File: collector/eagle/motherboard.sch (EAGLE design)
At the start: 9 parts

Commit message: Updated scheme of collector motherboard
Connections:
- net GND: now also U$3.LED_GREEN_-, U$3.LED_YELLOW_-
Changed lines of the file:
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@@
 <part name="U$1" library="ut-boards" deviceset="HANRUN_HR911105A_15/10" device=""/>
 <part name="U$2" library="ut-boards" deviceset="STM32F103C8T6_BOARD_BLACK" device=""/>
-<part name="U$3" library="ut-connectors" deviceset="RJHSE-5481_(RJ45)" device=""/>
 <part name="R1" library="resistor" deviceset="R-EU_" device="R1206"/>
 <part name="R2" library="resistor" deviceset="R-EU_" device="R1206"/>
@@
 <part name="R4" library="resistor" deviceset="R-EU_" device="R1206"/>
 <part name="R5" library="resistor" deviceset="R-EU_" device="R1206"/>
+<part name="U$3" library="ut-connectors" deviceset="RJHSE-5481_(RJ45)" device=""/>
 </parts>
 <sheets>
@@
 <instance part="U$1" gate="G$1" x="40.64" y="60.96" rot="R270"/>
 <instance part="U$2" gate="G$1" x="104.14" y="43.18"/>
-<instance part="U$3" gate="G$1" x="101.6" y="-35.56"/>
 <instance part="R1" gate="G$1" x="121.92" y="-12.7"/>
 <instance part="R2" gate="G$1" x="121.92" y="-10.16"/>
@@
 <instance part="R4" gate="G$1" x="76.2" y="33.02"/>
 <instance part="R5" gate="G$1" x="76.2" y="38.1"/>
+<instance part="U$3" gate="G$1" x="101.6" y="-35.56"/>
 </instances>
 <busses>
@@
 <wire x1="119.38" y1="-20.32" x2="93.98" y2="-20.32" width="0.1524" layer="91"/>
 <wire x1="93.98" y1="-20.32" x2="88.9" y2="-20.32" width="0.1524" layer="91"/>
-<wire x1="88.9" y1="-20.32" x2="88.9" y2="-22.86" width="0.1524" layer="91"/>
-<wire x1="119.38" y1="-20.32" x2="119.38" y2="-22.86" width="0.1524" layer="91"/>
 <junction x="88.9" y="-20.32"/>
 <wire x1="129.54" y1="-20.32" x2="119.38" y2="-20.32" width="0.1524" layer="91"/>
@@
 <wire x1="93.98" y1="-33.02" x2="93.98" y2="-20.32" width="0.1524" layer="91"/>
 <junction x="93.98" y="-20.32"/>
-<pinref part="U$3" gate="G$1" pin="P8"/>
 <wire x1="88.9" y1="-20.32" x2="35.56" y2="-20.32" width="0.1524" layer="91"/>
 <wire x1="35.56" y1="-20.32" x2="35.56" y2="45.72" width="0.1524" layer="91"/>
@@
 <label x="124.46" y="-22.86" size="1.778" layer="95"/>
 <label x="101.6" y="-20.32" size="1.778" layer="95"/>
+<pinref part="U$3" gate="G$1" pin="P8"/>
+<pinref part="U$3" gate="G$1" pin="LED_YELLOW_-"/>
+<wire x1="88.9" y1="-20.32" x2="88.9" y2="-27.94" width="0.1524" layer="91"/>
+<pinref part="U$3" gate="G$1" pin="LED_GREEN_-"/>
+<wire x1="119.38" y1="-20.32" x2="119.38" y2="-27.94" width="0.1524" layer="91"/>
 </segment>
 </net>
@@
 <wire x1="116.84" y1="27.94" x2="96.52" y2="27.94" width="0.1524" layer="91"/>
 <wire x1="96.52" y1="27.94" x2="96.52" y2="-2.54" width="0.1524" layer="91"/>
-<pinref part="U$3" gate="G$1" pin="P7"/>
 <wire x1="96.52" y1="-2.54" x2="96.52" y2="-35.56" width="0.1524" layer="91"/>
 <wire x1="96.52" y1="-2.54" x2="38.1" y2="-2.54" width="0.1524" layer="91"/>
@@
 <label x="76.2" y="-5.08" size="1.778" layer="95"/>
 <label x="96.52" y="-15.24" size="1.778" layer="95"/>
+<pinref part="U$3" gate="G$1" pin="P7"/>
 </segment>
 </net>
@@
 <net name="N$9" class="0">
 <segment>
-<wire x1="116.84" y1="-12.7" x2="116.84" y2="-22.86" width="0.1524" layer="91"/>
+<wire x1="116.84" y1="-12.7" x2="116.84" y2="-27.94" width="0.1524" layer="91"/>
+<pinref part="R1" gate="G$1" pin="1"/>
 <pinref part="U$3" gate="G$1" pin="LED_GREEN_+"/>
-<pinref part="R1" gate="G$1" pin="1"/>
-<wire x1="116.84" y1="-27.94" x2="116.84" y2="-22.86" width="0.1524" layer="91"/>
 </segment>
 </net>
@@
 <segment>
 <wire x1="86.36" y1="-10.16" x2="86.36" y2="-27.94" width="0.1524" layer="91"/>
-<pinref part="U$3" gate="G$1" pin="LED_YELLOW_+"/>
 <pinref part="R2" gate="G$1" pin="1"/>
 <wire x1="116.84" y1="-10.16" x2="86.36" y2="-10.16" width="0.1524" layer="91"/>
 <label x="101.6" y="-10.16" size="1.778" layer="95"/>
+<pinref part="U$3" gate="G$1" pin="LED_YELLOW_+"/>
 </segment>
 </net>
@@
 <junction x="91.44" y="58.42"/>
 <wire x1="111.76" y1="58.42" x2="111.76" y2="-35.56" width="0.1524" layer="91"/>
+<label x="111.76" y="-2.54" size="1.778" layer="95"/>
 <pinref part="U$3" gate="G$1" pin="P1"/>
-<label x="111.76" y="-2.54" size="1.778" layer="95"/>
 </segment>
 </net>
@@
 <junction x="91.44" y="55.88"/>
 <wire x1="109.22" y1="55.88" x2="109.22" y2="-33.02" width="0.1524" layer="91"/>
+<label x="104.14" y="-2.54" size="1.778" layer="95"/>
 <pinref part="U$3" gate="G$1" pin="P2"/>
-<label x="104.14" y="-2.54" size="1.778" layer="95"/>
 </segment>
 </net>

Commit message: Tiny fixes on colletor's motherboard
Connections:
- net 3V3: now also RGB_LED.4
- net GND: no longer RGB_LED.4
- net PC13: now also RGB_LED.3; no longer RGB_LED.1
- net PC15: now also RGB_LED.1; no longer RGB_LED.3
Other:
- note added: "+"
- note removed: "GND"
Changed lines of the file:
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@@
 <text x="66.04" y="17.78" size="1.778" layer="97">G</text>
 <text x="60.96" y="15.24" size="1.778" layer="97">B</text>
-<text x="66.04" y="15.24" size="1.778" layer="97">GND</text>
+<text x="65.532" y="13.716" size="1.778" layer="97">+</text>
 </plain>
 <instances>
@@
 <wire x1="129.54" y1="-20.32" x2="119.38" y2="-20.32" width="0.1524" layer="91"/>
 <junction x="119.38" y="-20.32"/>
-<pinref part="RGB_LED" gate="A" pin="4"/>
-<wire x1="66.04" y1="15.24" x2="116.84" y2="15.24" width="0.1524" layer="91"/>
-<junction x="116.84" y="15.24"/>
 <wire x1="93.98" y1="-33.02" x2="93.98" y2="-20.32" width="0.1524" layer="91"/>
 <junction x="93.98" y="-20.32"/>
@@
 <junction x="116.84" y="27.94"/>
 <wire x1="116.84" y1="27.94" x2="96.52" y2="27.94" width="0.1524" layer="91"/>
-<wire x1="96.52" y1="27.94" x2="96.52" y2="-2.54" width="0.1524" layer="91"/>
+<wire x1="96.52" y1="27.94" x2="96.52" y2="15.24" width="0.1524" layer="91"/>
+<wire x1="96.52" y1="15.24" x2="96.52" y2="-2.54" width="0.1524" layer="91"/>
 <wire x1="96.52" y1="-2.54" x2="96.52" y2="-35.56" width="0.1524" layer="91"/>
 <wire x1="96.52" y1="-2.54" x2="38.1" y2="-2.54" width="0.1524" layer="91"/>
@@
 <label x="96.52" y="-15.24" size="1.778" layer="95"/>
 <pinref part="U$3" gate="G$1" pin="P7"/>
+<pinref part="RGB_LED" gate="A" pin="4"/>
+<wire x1="96.52" y1="15.24" x2="66.04" y2="15.24" width="0.1524" layer="91"/>
+<junction x="96.52" y="15.24"/>
 </segment>
 </net>
@@
 <net name="PC13" class="0">
 <segment>
-<pinref part="RGB_LED" gate="A" pin="1"/>
-<wire x1="55.88" y1="38.1" x2="55.88" y2="17.78" width="0.1524" layer="91"/>
-<wire x1="55.88" y1="17.78" x2="58.42" y2="17.78" width="0.1524" layer="91"/>
 <pinref part="R5" gate="G$1" pin="1"/>
-<wire x1="71.12" y1="38.1" x2="55.88" y2="38.1" width="0.1524" layer="91"/>
-<label x="55.88" y="25.4" size="1.778" layer="95"/>
+<wire x1="71.12" y1="38.1" x2="53.34" y2="38.1" width="0.1524" layer="91"/>
+<wire x1="53.34" y1="38.1" x2="53.34" y2="15.24" width="0.1524" layer="91"/>
+<pinref part="RGB_LED" gate="A" pin="3"/>
+<wire x1="53.34" y1="15.24" x2="58.42" y2="15.24" width="0.1524" layer="91"/>
+<label x="55.88" y="35.56" size="1.778" layer="95"/>
 </segment>
 </net>
@@
 </segment>
 </net>
-<net name="PC15" class="0">
-<segment>
-<pinref part="RGB_LED" gate="A" pin="3"/>
-<wire x1="50.8" y1="33.02" x2="50.8" y2="15.24" width="0.1524" layer="91"/>
-<wire x1="50.8" y1="15.24" x2="58.42" y2="15.24" width="0.1524" layer="91"/>
-<pinref part="R4" gate="G$1" pin="1"/>
-<wire x1="71.12" y1="33.02" x2="50.8" y2="33.02" width="0.1524" layer="91"/>
-<label x="43.18" y="17.78" size="1.778" layer="95"/>
-</segment>
-</net>
 <net name="N$16" class="0">
 <segment>
@@
 </segment>
 </net>
+<net name="PC15" class="0">
+<segment>
+<pinref part="R4" gate="G$1" pin="1"/>
+<wire x1="71.12" y1="33.02" x2="55.88" y2="33.02" width="0.1524" layer="91"/>
+<wire x1="55.88" y1="33.02" x2="55.88" y2="17.78" width="0.1524" layer="91"/>
+<pinref part="RGB_LED" gate="A" pin="1"/>
+<wire x1="55.88" y1="17.78" x2="58.42" y2="17.78" width="0.1524" layer="91"/>
+<label x="58.42" y="30.48" size="1.778" layer="95"/>
+</segment>
+</net>

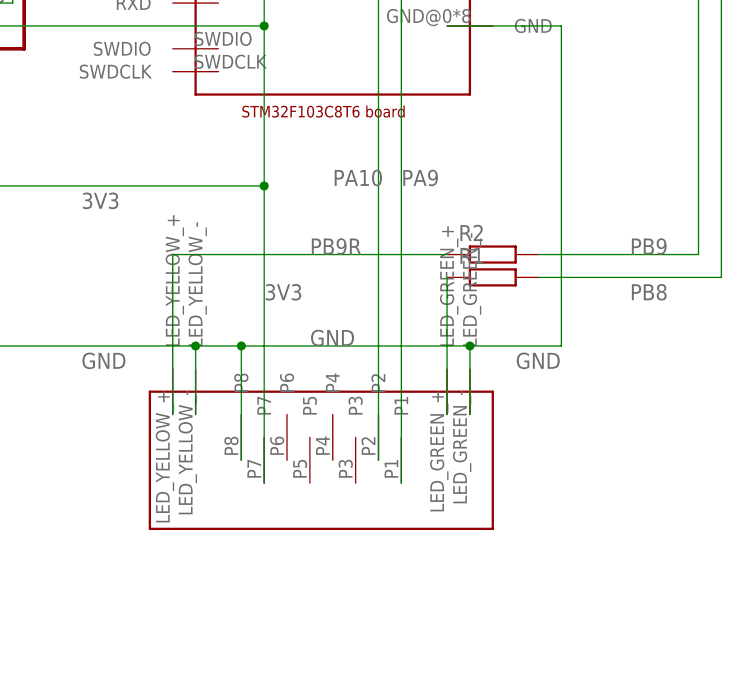
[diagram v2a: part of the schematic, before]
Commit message: Updated sensor's scheme, colletor's photo and README.md
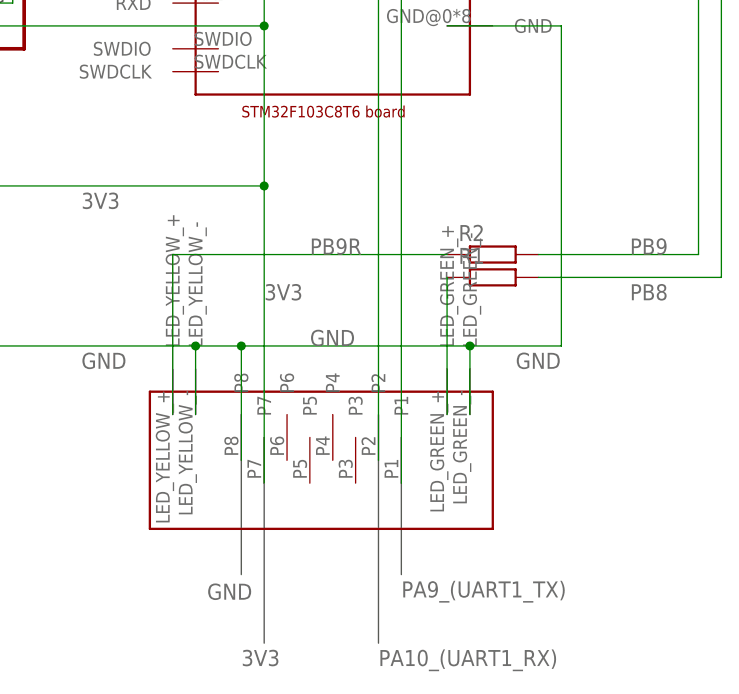
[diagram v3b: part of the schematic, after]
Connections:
- net PA10 renamed PA10_(UART1_RX)
- net PA9 renamed PA9_(UART1_TX)
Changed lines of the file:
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@@
 <text x="60.96" y="15.24" size="1.778" layer="97">B</text>
 <text x="65.532" y="13.716" size="1.778" layer="97">+</text>
+<wire x1="93.98" y1="-33.02" x2="93.98" y2="-45.72" width="0.1524" layer="97"/>
+<wire x1="96.52" y1="-53.34" x2="96.52" y2="-35.56" width="0.1524" layer="97"/>
+<wire x1="109.22" y1="-33.02" x2="109.22" y2="-53.34" width="0.1524" layer="97"/>
+<wire x1="111.76" y1="-35.56" x2="111.76" y2="-45.72" width="0.1524" layer="97"/>
 </plain>
 <instances>
@@
 <pinref part="U$3" gate="G$1" pin="LED_GREEN_-"/>
 <wire x1="119.38" y1="-20.32" x2="119.38" y2="-27.94" width="0.1524" layer="91"/>
+<label x="90.17" y="-48.514" size="1.778" layer="95"/>
 </segment>
 </net>
@@
 <wire x1="96.52" y1="15.24" x2="66.04" y2="15.24" width="0.1524" layer="91"/>
 <junction x="96.52" y="15.24"/>
+<label x="93.98" y="-55.88" size="1.778" layer="95"/>
 </segment>
 </net>
@@
 </segment>
 </net>
-<net name="PA9" class="0">
+<net name="PA9_(UART1_TX)" class="0">
 <segment>
 <pinref part="U$2" gate="G$1" pin="PA9"/>
@@
 <junction x="91.44" y="58.42"/>
 <wire x1="111.76" y1="58.42" x2="111.76" y2="-35.56" width="0.1524" layer="91"/>
-<label x="111.76" y="-2.54" size="1.778" layer="95"/>
 <pinref part="U$3" gate="G$1" pin="P1"/>
+<label x="111.76" y="-48.26" size="1.778" layer="95"/>
 </segment>
 </net>
-<net name="PA10" class="0">
+<net name="PA10_(UART1_RX)" class="0">
 <segment>
 <pinref part="U$2" gate="G$1" pin="PA10"/>
@@
 <junction x="91.44" y="55.88"/>
 <wire x1="109.22" y1="55.88" x2="109.22" y2="-33.02" width="0.1524" layer="91"/>
-<label x="104.14" y="-2.54" size="1.778" layer="95"/>
 <pinref part="U$3" gate="G$1" pin="P2"/>
+<label x="109.22" y="-55.88" size="1.778" layer="95"/>
 </segment>
 </net>

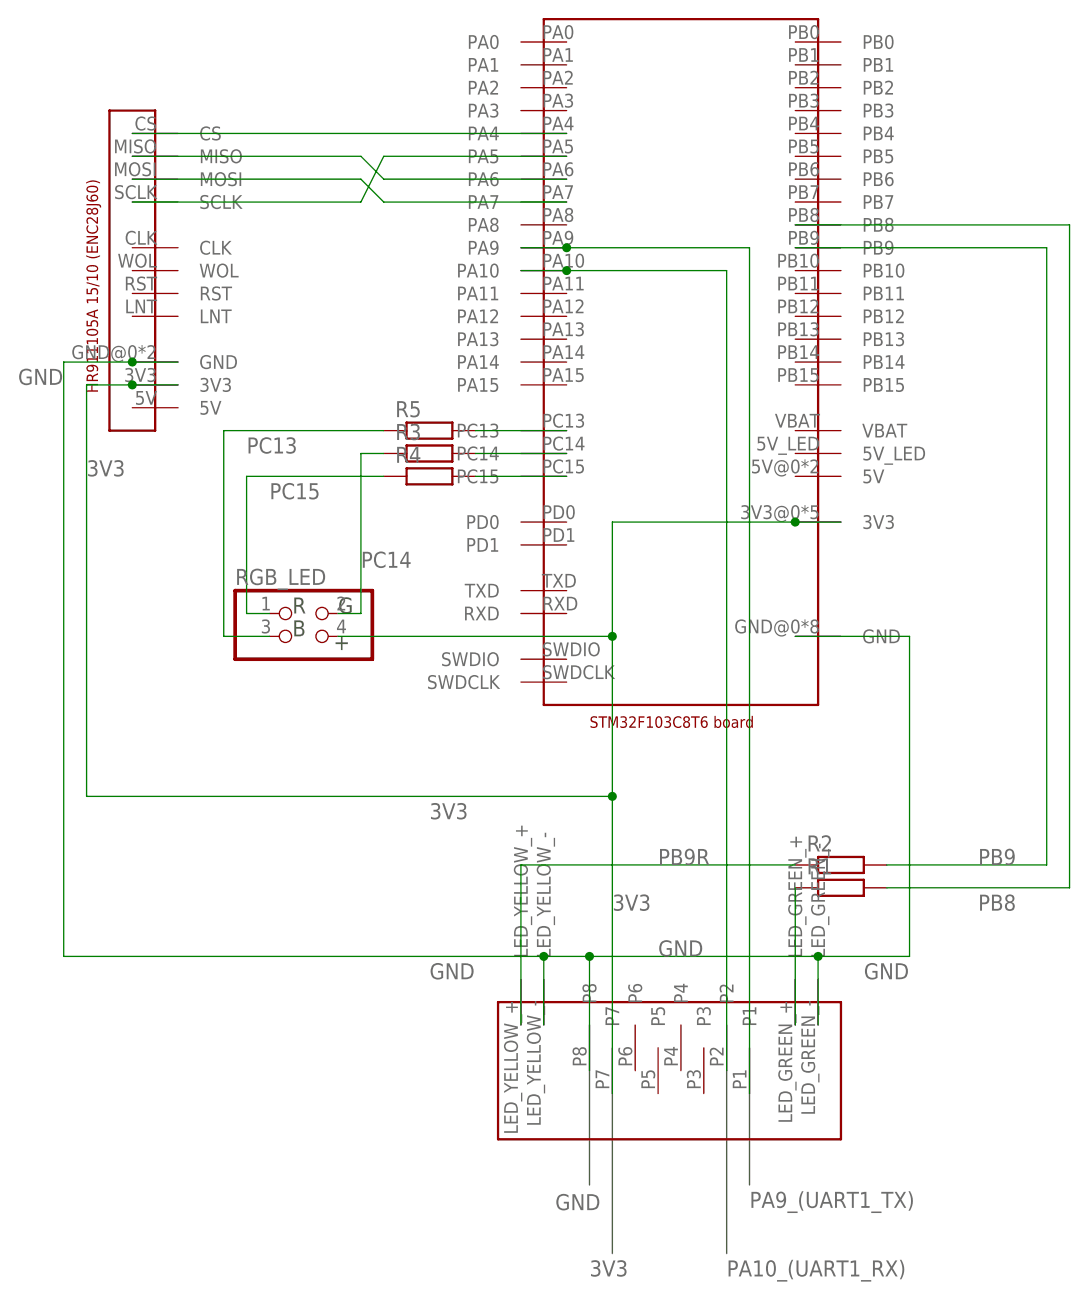
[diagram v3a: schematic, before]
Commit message: Added a pull-up resistor for UART-RX of collector
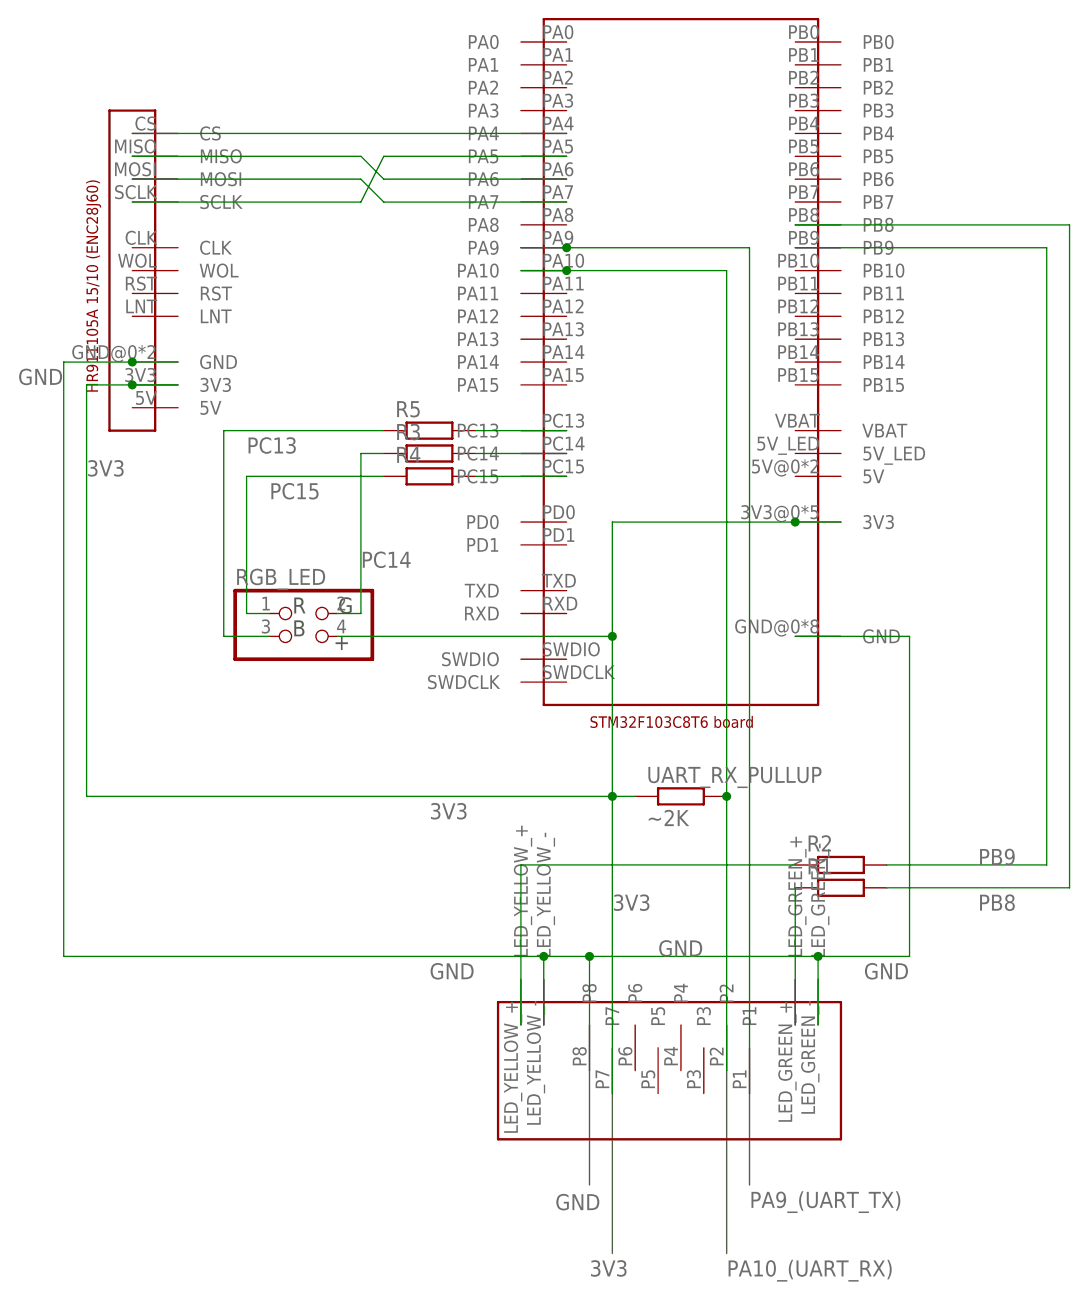
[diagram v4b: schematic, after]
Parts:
- added UART_RX_PULLUP: ~2K, resistor:R-EU_R1206
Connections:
- net PA9_(UART1_TX) renamed PA9_(UART_TX)
- removed net PA10_(UART1_RX): U$2.PA10, U$3.P2
- new net PA10_(UART_RX): U$2.PA10, U$3.P2, UART_RX_PULLUP.2
- net 3V3: now also UART_RX_PULLUP.1
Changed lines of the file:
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@@
 <part name="R5" library="resistor" deviceset="R-EU_" device="R1206"/>
 <part name="U$3" library="ut-connectors" deviceset="RJHSE-5481_(RJ45)" device=""/>
+<part name="UART_RX_PULLUP" library="resistor" deviceset="R-EU_" device="R1206" value="~2K"/>
 </parts>
 <sheets>
@@
 <instance part="R5" gate="G$1" x="76.2" y="38.1"/>
 <instance part="U$3" gate="G$1" x="101.6" y="-35.56"/>
+<instance part="UART_RX_PULLUP" gate="G$1" x="104.14" y="-2.54"/>
 </instances>
 <busses>
@@
 <junction x="96.52" y="15.24"/>
 <label x="93.98" y="-55.88" size="1.778" layer="95"/>
+<pinref part="UART_RX_PULLUP" gate="G$1" pin="1"/>
+<wire x1="99.06" y1="-2.54" x2="96.52" y2="-2.54" width="0.1524" layer="91"/>
 </segment>
 </net>
@@
 <pinref part="R2" gate="G$1" pin="1"/>
 <wire x1="116.84" y1="-10.16" x2="86.36" y2="-10.16" width="0.1524" layer="91"/>
-<label x="101.6" y="-10.16" size="1.778" layer="95"/>
 <pinref part="U$3" gate="G$1" pin="LED_YELLOW_+"/>
-</segment>
-</net>
-<net name="PA9_(UART1_TX)" class="0">
-<segment>
-<pinref part="U$2" gate="G$1" pin="PA9"/>
-<wire x1="86.36" y1="58.42" x2="91.44" y2="58.42" width="0.1524" layer="91"/>
-<wire x1="91.44" y1="58.42" x2="111.76" y2="58.42" width="0.1524" layer="91"/>
-<junction x="91.44" y="58.42"/>
-<wire x1="111.76" y1="58.42" x2="111.76" y2="-35.56" width="0.1524" layer="91"/>
-<pinref part="U$3" gate="G$1" pin="P1"/>
-<label x="111.76" y="-48.26" size="1.778" layer="95"/>
-</segment>
-</net>
-<net name="PA10_(UART1_RX)" class="0">
-<segment>
-<pinref part="U$2" gate="G$1" pin="PA10"/>
-<wire x1="86.36" y1="55.88" x2="91.44" y2="55.88" width="0.1524" layer="91"/>
-<wire x1="91.44" y1="55.88" x2="109.22" y2="55.88" width="0.1524" layer="91"/>
-<junction x="91.44" y="55.88"/>
-<wire x1="109.22" y1="55.88" x2="109.22" y2="-33.02" width="0.1524" layer="91"/>
-<pinref part="U$3" gate="G$1" pin="P2"/>
-<label x="109.22" y="-55.88" size="1.778" layer="95"/>
 </segment>
 </net>
@@
 </segment>
 </net>
+<net name="PA9_(UART_TX)" class="0">
+<segment>
+<pinref part="U$2" gate="G$1" pin="PA9"/>
+<wire x1="86.36" y1="58.42" x2="91.44" y2="58.42" width="0.1524" layer="91"/>
+<wire x1="91.44" y1="58.42" x2="111.76" y2="58.42" width="0.1524" layer="91"/>
+<wire x1="111.76" y1="58.42" x2="111.76" y2="-35.56" width="0.1524" layer="91"/>
+<junction x="91.44" y="58.42"/>
+<pinref part="U$3" gate="G$1" pin="P1"/>
+<label x="111.76" y="-48.26" size="1.778" layer="95"/>
+</segment>
+</net>
+<net name="PA10_(UART_RX)" class="0">
+<segment>
+<pinref part="U$2" gate="G$1" pin="PA10"/>
+<wire x1="86.36" y1="55.88" x2="91.44" y2="55.88" width="0.1524" layer="91"/>
+<wire x1="91.44" y1="55.88" x2="109.22" y2="55.88" width="0.1524" layer="91"/>
+<wire x1="109.22" y1="55.88" x2="109.22" y2="-2.54" width="0.1524" layer="91"/>
+<junction x="91.44" y="55.88"/>
+<pinref part="U$3" gate="G$1" pin="P2"/>
+<label x="109.22" y="-55.88" size="1.778" layer="95"/>
+<pinref part="UART_RX_PULLUP" gate="G$1" pin="2"/>
+<wire x1="109.22" y1="-2.54" x2="109.22" y2="-33.02" width="0.1524" layer="91"/>
+<junction x="109.22" y="-2.54"/>
+</segment>
+</net>
